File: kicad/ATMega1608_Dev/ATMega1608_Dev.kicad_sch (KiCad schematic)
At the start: 37 parts, among them J1 Alt Power, J101 GPIO2, J2 USB_B_Micro, J3 Comm, J4 GPIO1, J6 Power OUT, U1 TC1262-33, U2 FT232RQ, U3 ATMega1608_32

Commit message: Removes the FT232 and replaces with a UM2102N port
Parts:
- removed C1: 10nF, Capacitor_SMD:C_0805_2012Metric, symbol Device:C
- removed C2, C4: 100nF, Capacitor_SMD:C_0805_2012Metric, symbol Device:C
- removed C3: 4.7μF, Capacitor_SMD:C_1206_3216Metric, symbol Device:C
- removed D4: RED_GREEN, atmega1608_footprints:LED_KKAA_15-22SURSYGC, symbol atmega1608_dev:LED_Dual_KKAA
- removed J1: Alt Power, Connector_PinHeader_2.54mm:PinHeader_1x02_P2.54mm_Vertical, symbol Connector:Conn_01x02_Male
- removed J2: USB_B_Micro, atmega1608_footprints:USB_Micro-B_Amphenol_10103594-0001LF_Horizontal, symbol Connector:USB_B_Micro
- removed L1: 33Ω, Inductor_SMD:L_1206_3216Metric, symbol Device:L
- removed R1, R3, R4: 0Ω, Resistor_SMD:R_0805_2012Metric, symbol Device:R
- removed R5, R6: NOPOP, Resistor_SMD:R_0805_2012Metric, symbol Device:R
- removed R7, R8: 270Ω, Resistor_SMD:R_0805_2012Metric, symbol Device:R
- removed U2: FT232RQ, Package_DFN_QFN:QFN-32-1EP_5x5mm_P0.5mm_EP3.3x3.3mm_ThermalVias, symbol atmega1608_dev:FT232RQ
- added J1: Alt Power, Connector_PinHeader_2.54mm:PinHeader_1x02_P2.54mm_Vertical, symbol Connector:Conn_01x02_Pin
- added J2: USART-USB, Connector_PinSocket_2.54mm:PinSocket_1x06_P2.54mm_Vertical, symbol Connector:Conn_01x06_Socket
- J3: renamed from J4; symbol Connector:Conn_01x08_Male -> Connector:Conn_01x08_Pin
- J4: renamed from J6; symbol Connector:Conn_01x02_Male -> Connector:Conn_01x02_Pin
- J5: renamed from J101; symbol Connector:Conn_01x12_Male -> Connector:Conn_01x12_Pin
- J6: renamed from J3; symbol Connector:Conn_01x08_Male -> Connector:Conn_01x08_Pin
- renumbered C7 to C6, C8 to C7, LG3 to LG2, R9 to R10, R10 to R11, R11 to R12
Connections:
- net DIN: now also J2.2 (Pin_2)
- net DOUT: now also J2.3 (Pin_3)
- net GND: now also U3.19 (GND), U3.29 (GND), J1.2 (Pin_2), J2.4 (Pin_4)
- net USB-5V: now reaches D2.2 (A)
- net USB-5V: now also J2.5 (Pin_5)
- net at D1.2 (A): now also J1.1 (Pin_1)
- net +3V3 renamed +3.3V
- no-connect marks 19 -> 5
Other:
- note removed: "5mA"
- moved on the sheet: C5, D1, D2, D3, J3, J4, J5, J6, R10, R2, TC1, U1

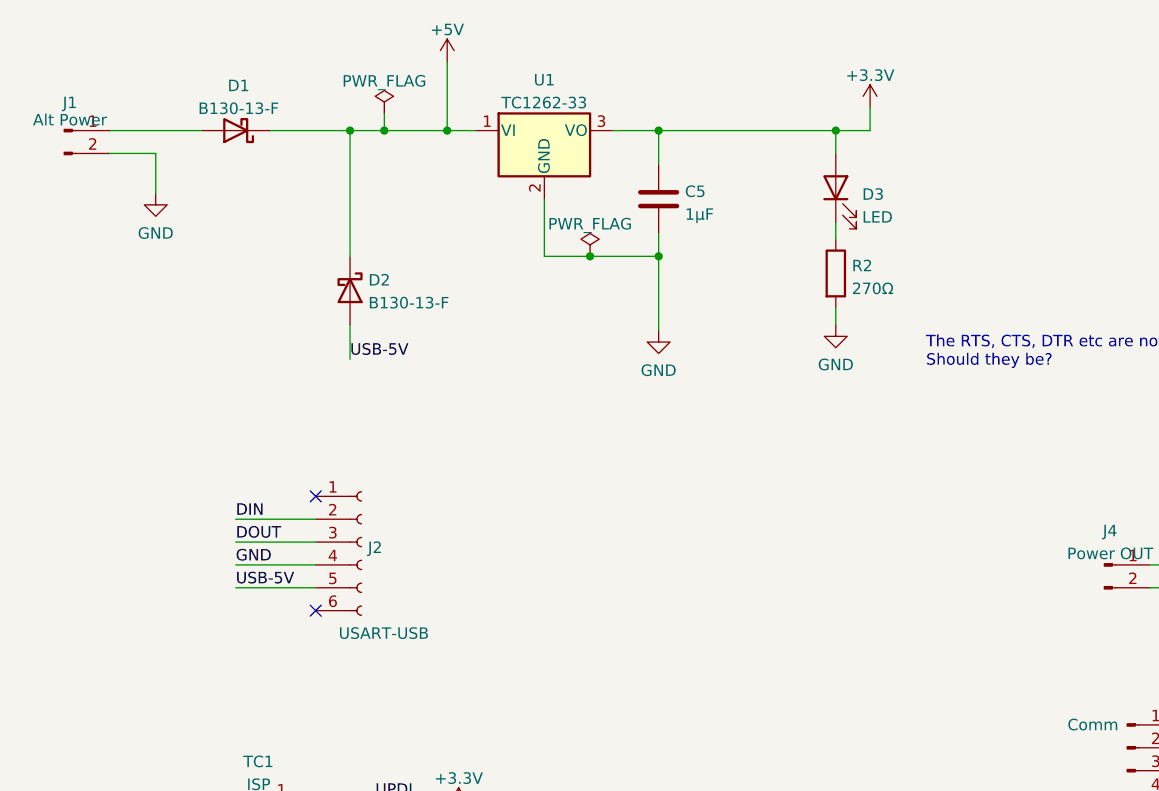
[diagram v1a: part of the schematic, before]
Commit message: Fixes label overflow
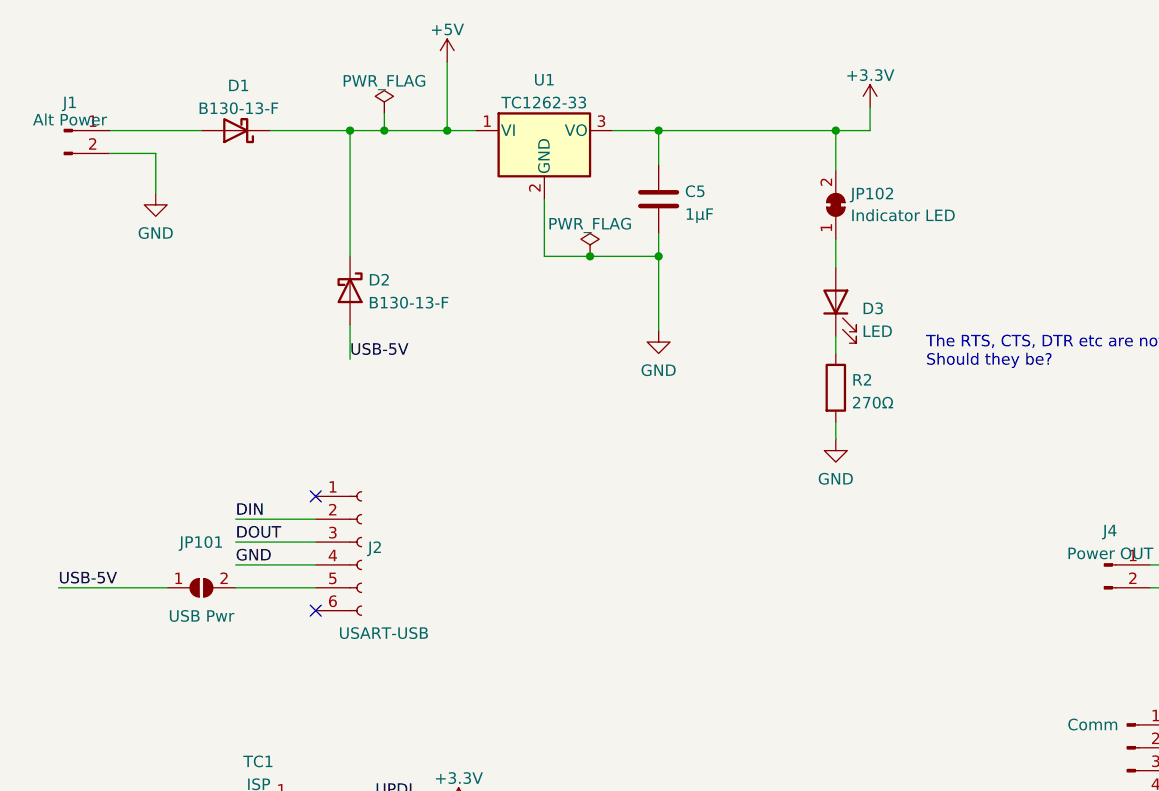
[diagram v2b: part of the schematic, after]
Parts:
- added JP101: USB Pwr, Connector_PinHeader_2.54mm:PinHeader_1x02_P2.54mm_Vertical, symbol Jumper:SolderJumper_2_Open
- added JP102: Indicator LED, Jumper:SolderJumper-2_P1.3mm_Bridged_RoundedPad1.0x1.5mm, symbol Jumper:SolderJumper_2_Bridged
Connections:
- net +3.3V: now also JP102.2 (B); no longer D3.2 (A)
- net USB-5V: now also JP101.1 (A); no longer J2.5 (Pin_5)
- new net: J2.5 (Pin_5), JP101.2 (B)
- new net: D3.2 (A), JP102.1 (A)
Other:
- moved on the sheet: D3, R2
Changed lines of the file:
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@@
     (stroke (width 0) (type default))
   )
-  (wire (pts (xy 113.03 31.75) (xy 113.03 34.29))
+  (wire (pts (xy 113.03 31.75) (xy 113.03 36.195))
     (stroke (width 0) (type default))
   )
@@
     (stroke (width 0) (type default))
   )
+  (wire (pts (xy 26.67 82.55) (xy 38.735 82.55))
+    (stroke (width 0) (type default))
+  )
   (wire (pts (xy 37.465 34.29) (xy 37.465 38.735))
     (stroke (width 0) (type default))
@@
     (stroke (width 0) (type default))
   )
-  (wire (pts (xy 113.03 41.91) (xy 113.03 43.815))
+  (wire (pts (xy 113.03 54.61) (xy 113.03 56.515))
     (stroke (width 0) (type default))
   )
@@
     (stroke (width 0) (type default))
   )
-  (wire (pts (xy 113.03 51.435) (xy 113.03 53.34))
+  (wire (pts (xy 113.03 64.135) (xy 113.03 66.04))
     (stroke (width 0) (type default))
   )
@@
   )
   (wire (pts (xy 317.5 140.335) (xy 337.82 140.335))
+    (stroke (width 0) (type default))
+  )
+  (wire (pts (xy 113.03 43.815) (xy 113.03 46.99))
     (stroke (width 0) (type default))
   )
@@
     (effects (font (size 1.27 1.27)) (justify left bottom))
   )
-  (label "USB-5V" (at 46.355 82.55 0) (fields_autoplaced)
+  (label "USB-5V" (at 26.67 82.55 0) (fields_autoplaced)
     (effects (font (size 1.27 1.27)) (justify left bottom))
   )
@@
         (path "/23ade321-bb44-4926-846a-ff20dfe7a942"
           (reference "#PWR012") (unit 1)
+        )
+      )
+    )
+  )
+  (symbol (lib_id "Jumper:SolderJumper_2_Open") (at 42.545 82.55 0) (unit 1)
+    (in_bom yes) (on_board yes) (dnp no)
+    (property "Reference" "JP101" (at 42.545 77.5167 0)
+      (effects (font (size 1.27 1.27)))
+    )
+    (property "Value" "USB Pwr" (at 42.545 85.725 0)
+      (effects (font (size 1.27 1.27)))
+    )
+    (property "Footprint" "Connector_PinHeader_2.54mm:PinHeader_1x02_P2.54mm_Vertical" (at 42.545 82.55 0)
+      (effects (font (size 1.27 1.27)) hide)
+    )
+    (property "Datasheet" "~" (at 42.545 82.55 0)
+      (effects (font (size 1.27 1.27)) hide)
+    )
+    (pin "1")
+    (pin "2")
+    (instances
+      (project "ATMega1608_Dev"
+        (path "/23ade321-bb44-4926-846a-ff20dfe7a942"
+          (reference "JP101") (unit 1)
         )
       )
@@
     )
   )
-  (symbol (lib_id "Device:R") (at 113.03 47.625 0) (unit 1)
-    (in_bom yes) (on_board yes) (dnp no) (fields_autoplaced)
-    (property "Reference" "R2" (at 114.808 46.7903 0)
-      (effects (font (size 1.27 1.27)) (justify left))
-    )
-    (property "Value" "270Ω" (at 114.808 49.3272 0)
-      (effects (font (size 1.27 1.27)) (justify left))
-    )
-    (property "Footprint" "Resistor_SMD:R_0805_2012Metric" (at 111.252 47.625 90)
-      (effects (font (size 1.27 1.27)) hide)
-    )
-    (property "Datasheet" "~" (at 113.03 47.625 0)
+  (symbol (lib_id "Device:R") (at 113.03 60.325 0) (unit 1)
+    (in_bom yes) (on_board yes) (dnp no) (fields_autoplaced)
+    (property "Reference" "R2" (at 114.808 59.4903 0)
+      (effects (font (size 1.27 1.27)) (justify left))
+    )
+    (property "Value" "270Ω" (at 114.808 62.0272 0)
+      (effects (font (size 1.27 1.27)) (justify left))
+    )
+    (property "Footprint" "Resistor_SMD:R_0805_2012Metric" (at 111.252 60.325 90)
+      (effects (font (size 1.27 1.27)) hide)
+    )
+    (property "Datasheet" "~" (at 113.03 60.325 0)
       (effects (font (size 1.27 1.27)) hide)
     )
@@
     )
   )
-  (symbol (lib_id "Device:LED") (at 113.03 38.1 90) (unit 1)
-    (in_bom yes) (on_board yes) (dnp no) (fields_autoplaced)
-    (property "Reference" "D3" (at 115.951 38.8528 90)
+  (symbol (lib_id "Device:LED") (at 113.03 50.8 90) (unit 1)
+    (in_bom yes) (on_board yes) (dnp no) (fields_autoplaced)
+    (property "Reference" "D3" (at 115.951 51.5528 90)
       (effects (font (size 1.27 1.27)) (justify right))
     )
-    (property "Value" "LED" (at 115.951 41.3897 90)
+    (property "Value" "LED" (at 115.951 54.0897 90)
       (effects (font (size 1.27 1.27)) (justify right))
     )
-    (property "Footprint" "LED_SMD:LED_0805_2012Metric" (at 113.03 38.1 0)
-      (effects (font (size 1.27 1.27)) hide)
-    )
-    (property "Datasheet" "~" (at 113.03 38.1 0)
+    (property "Footprint" "LED_SMD:LED_0805_2012Metric" (at 113.03 50.8 0)
+      (effects (font (size 1.27 1.27)) hide)
+    )
+    (property "Datasheet" "~" (at 113.03 50.8 0)
       (effects (font (size 1.27 1.27)) hide)
     )
@@
     )
   )
-  (symbol (lib_id "power:GND") (at 113.03 53.34 0) (unit 1)
+  (symbol (lib_id "power:GND") (at 113.03 66.04 0) (unit 1)
     (in_bom yes) (on_board yes) (dnp no)
-    (property "Reference" "#PWR09" (at 113.03 59.69 0)
-      (effects (font (size 1.27 1.27)) hide)
-    )
-    (property "Value" "GND" (at 113.03 57.785 0)
-      (effects (font (size 1.27 1.27)))
-    )
-    (property "Footprint" "" (at 113.03 53.34 0)
-      (effects (font (size 1.27 1.27)) hide)
-    )
-    (property "Datasheet" "" (at 113.03 53.34 0)
+    (property "Reference" "#PWR09" (at 113.03 72.39 0)
+      (effects (font (size 1.27 1.27)) hide)
+    )
+    (property "Value" "GND" (at 113.03 70.485 0)
+      (effects (font (size 1.27 1.27)))
+    )
+    (property "Footprint" "" (at 113.03 66.04 0)
+      (effects (font (size 1.27 1.27)) hide)
+    )
+    (property "Datasheet" "" (at 113.03 66.04 0)
       (effects (font (size 1.27 1.27)) hide)
     )
@@
         )
       )
+    )
+  )
+  (symbol (lib_id "Jumper:SolderJumper_2_Bridged") (at 113.03 40.005 90) (unit 1)
+    (in_bom yes) (on_board yes) (dnp no) (fields_autoplaced)
+    (property "Reference" "JP102" (at 114.681 38.7929 90)
+      (effects (font (size 1.27 1.27)) (justify right))
+    )
+    (property "Value" "Indicator LED" (at 114.681 41.2171 90)
+      (effects (font (size 1.27 1.27)) (justify right))
+    )
+    (property "Footprint" "Jumper:SolderJumper-2_P1.3mm_Bridged_RoundedPad1.0x1.5mm" (at 113.03 40.005 0)
+      (effects (font (size 1.27 1.27)) hide)
+    )
+    (property "Datasheet" "~" (at 113.03 40.005 0)
+      (effects (font (size 1.27 1.27)) hide)
+    )
+    (pin "1")
+    (pin "2")
+    (instances
+      (project "ATMega1608_Dev"
+        (path "/23ade321-bb44-4926-846a-ff20dfe7a942"
+          (reference "JP102") (unit 1)
+        )
+      )
